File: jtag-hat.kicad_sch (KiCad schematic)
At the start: 0 parts

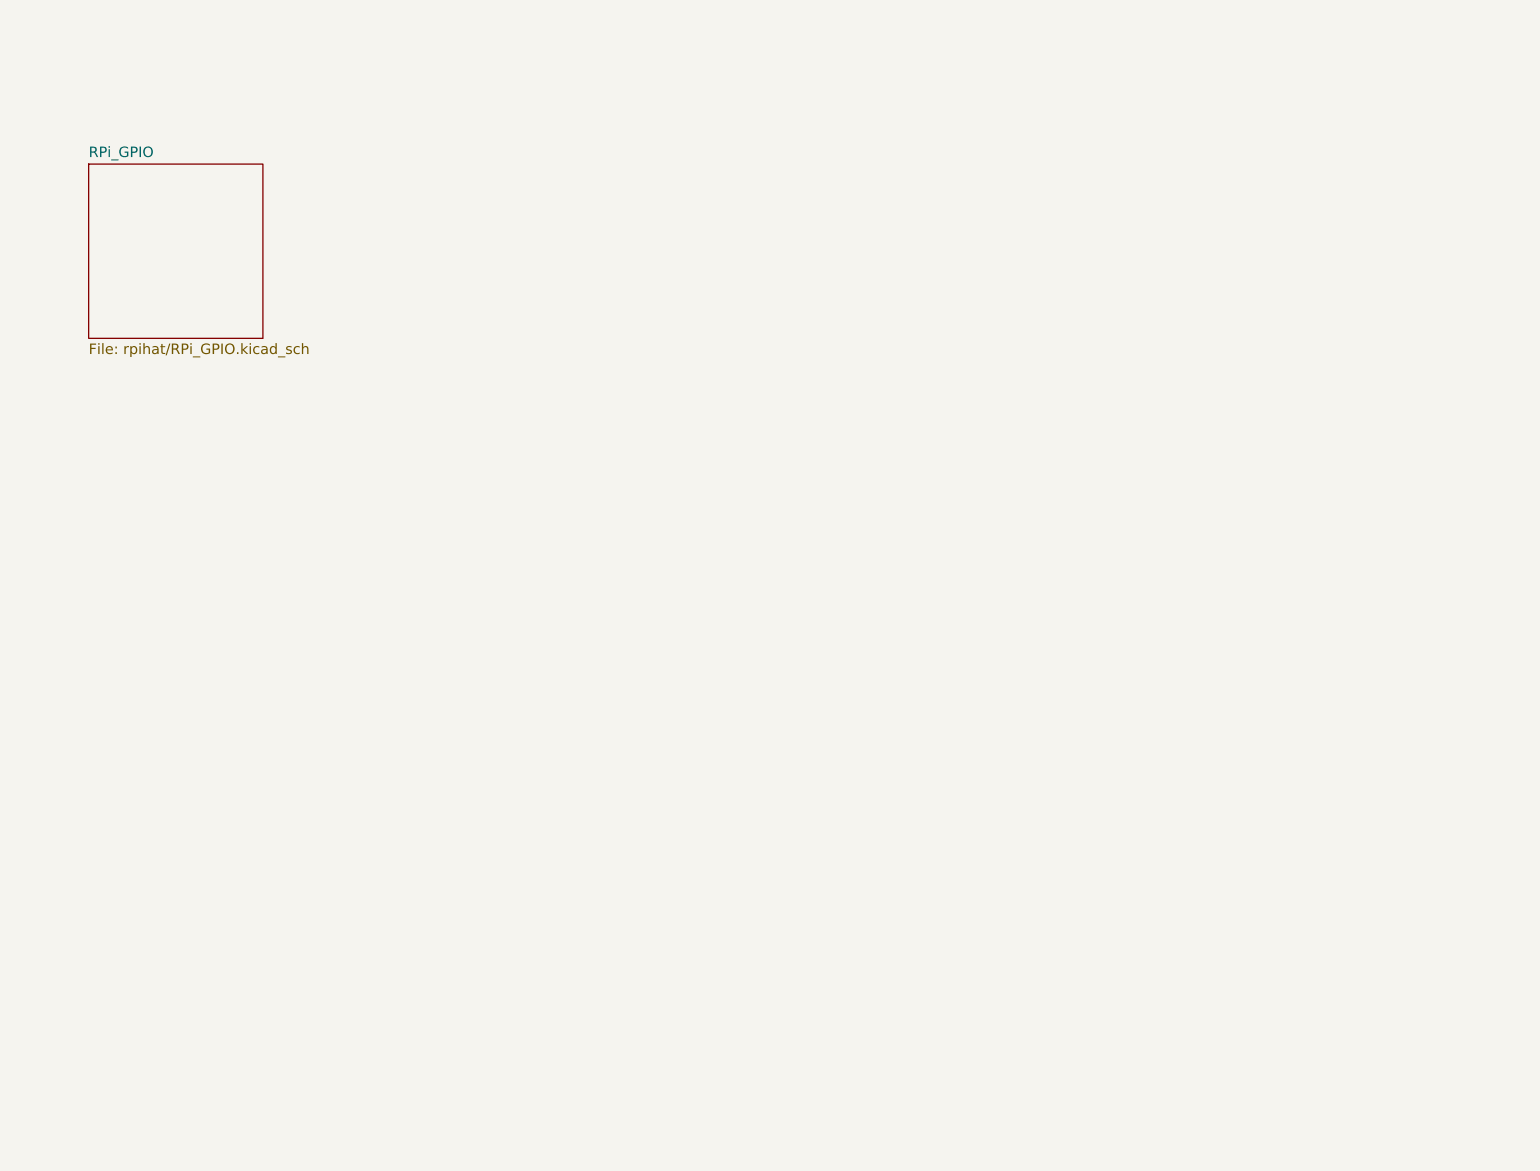
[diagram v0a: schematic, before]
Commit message: v1.5
- Changed mounting holes to 3.2mm (for M3)
- Swapped Pi-header for a straight pin-header
- Converted schematic from sub-schematic
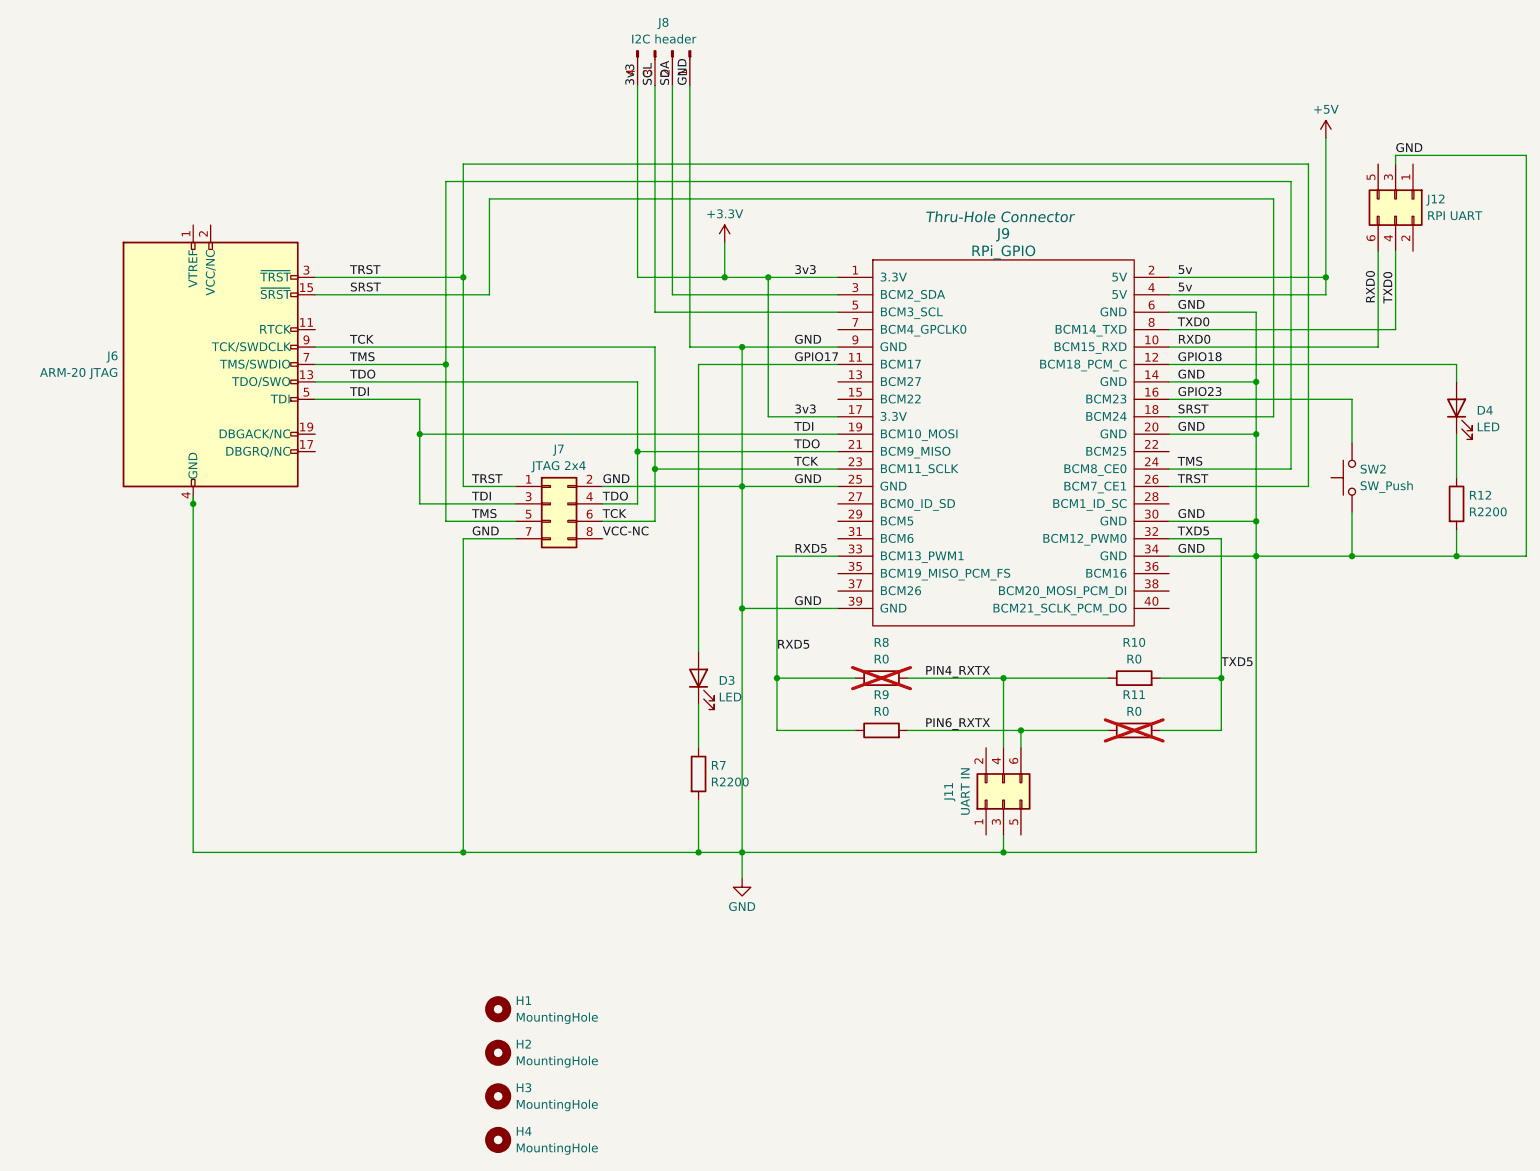
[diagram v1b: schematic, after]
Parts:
- added D3, D4: LED, LED_SMD:LED_0805_2012Metric_Pad1.15x1.40mm_HandSolder, symbol Device:LED
- added H1, H2, H3, H4: MountingHole, MountingHole:MountingHole_3.2mm_M3, symbol Mechanical:MountingHole
- added J11: UART IN, Connector_PinHeader_2.00mm:PinHeader_2x03_P2.00mm_Vertical_SMD, symbol Connector_Generic:Conn_02x03_Odd_Even
- added J12: RPI UART, Connector_PinHeader_2.00mm:PinHeader_2x03_P2.00mm_Vertical_SMD, symbol Connector_Generic:Conn_02x03_Odd_Even
- added J6: ARM-20 JTAG, Connector_PinHeader_2.54mm:PinHeader_2x10_P2.54mm_Vertical, symbol Connector:Conn_ARM_JTAG_SWD_20
- added J7: JTAG 2x4, Connector_PinHeader_2.00mm:PinHeader_2x04_P2.00mm_Vertical_SMD, symbol Connector_Generic:Conn_02x04_Odd_Even
- added J8: I2C header, Connector_PinHeader_2.54mm:PinHeader_1x04_P2.54mm_Vertical, symbol Connector:Conn_01x04_Pin
- added J9: RPi_GPIO, Connector_PinHeader_2.54mm:PinHeader_2x20_P2.54mm_Vertical, symbol RPi_Hat:RPi_GPIO
- added R10, R11, R8, R9: R0, Resistor_SMD:R_0402_1005Metric_Pad0.72x0.64mm_HandSolder, symbol Device:R
- added R12, R7: R2200, Resistor_SMD:R_0402_1005Metric_Pad0.72x0.64mm_HandSolder, symbol Device:R
- added SW2: SW_Push, Button_Switch_THT:SW_PUSH_6mm, symbol Switch:SW_Push
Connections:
- new net: D4.1 (K), R12.1
- new net: D3.1 (K), R7.1
- new net +3.3V: J8.4 (Pin_4), J9.1 (3.3V), J9.17 (3.3V)
- new net +5V: J9.2 (5V), J9.4 (5V)
- new net GND: J11.3 (Pin_3), J12.3 (Pin_3), J6.10 (GND), J6.12 (GND), J6.14 (GND), J6.16 (GND), J6.18 (GND), J6.20 (GND), J6.4 (GND), J6.6 (GND), J6.8 (GND), J7.2 (Pin_2), J7.7 (Pin_7), J8.1 (Pin_1), J9.14 (GND), J9.20 (GND), J9.25 (GND), J9.30 (GND), J9.34 (GND), J9.39 (GND), J9.6 (GND), J9.9 (GND), R12.2, R7.2, SW2.1
- new net GPIO17: D3.2 (A), J9.11 (BCM17)
- new net GPIO18: D4.2 (A), J9.12 (BCM18_PCM_C)
- new net GPIO23: J9.16 (BCM23), SW2.2
- new net PIN4_RXTX: J11.4 (Pin_4), R10.1, R8.2
- new net PIN6_RXTX: J11.6 (Pin_6), R11.1, R9.2
- new net RXD0: J12.6 (Pin_6), J9.10 (BCM15_RXD)
- new net RXD5: J9.33 (BCM13_PWM1), R8.1, R9.1
- new net SCL: J8.3 (Pin_3), J9.5 (BCM3_SCL)
- new net SDA: J8.2 (Pin_2), J9.3 (BCM2_SDA)
- new net SRST: J6.15 (~{SRST}), J9.18 (BCM24)
- new net TCK: J6.9 (TCK/SWDCLK), J7.6 (Pin_6), J9.23 (BCM11_SCLK)
- new net TDI: J6.5 (TDI), J7.3 (Pin_3), J9.19 (BCM10_MOSI)
- new net TDO: J6.13 (TDO/SWO), J7.4 (Pin_4), J9.21 (BCM9_MISO)
- new net TMS: J6.7 (TMS/SWDIO), J7.5 (Pin_5), J9.24 (BCM8_CE0)
- new net TRST: J6.3 (~{TRST}), J7.1 (Pin_1), J9.26 (BCM7_CE1)
- new net TXD0: J12.4 (Pin_4), J9.8 (BCM14_TXD)
- new net TXD5: J9.32 (BCM12_PWM0), R10.2, R11.2
- new net VCC-NC: J7.8 (Pin_8)
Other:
- removed sheet RPi_GPIO
- note added: "Thru-Hole Connector"
